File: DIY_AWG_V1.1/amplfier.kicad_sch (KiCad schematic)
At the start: 20 parts, among them IC3 LMH6505MAX, IC4 THS3091DDAR, J4 Conn_Coaxial

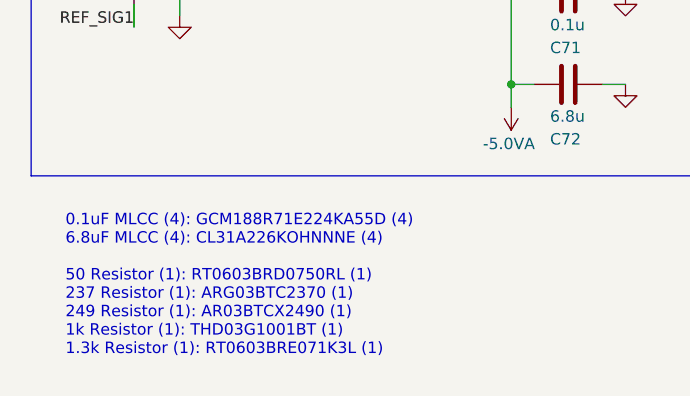
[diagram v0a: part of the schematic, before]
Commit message: Updated amplifier, STM32_MCU schematic
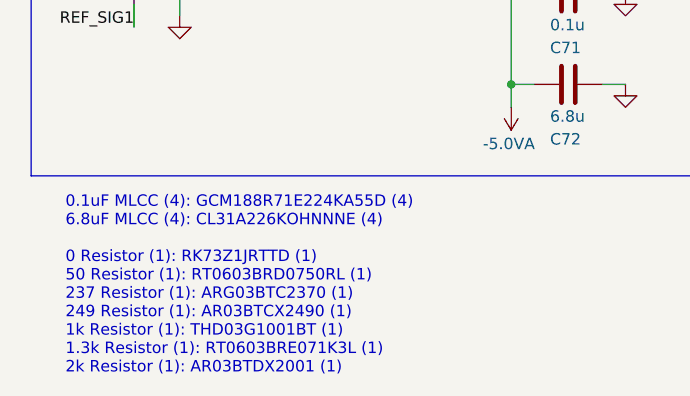
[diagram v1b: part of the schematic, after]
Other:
- note added: "0.1uF MLCC (4): GCM188R71E224KA55D (4) 6.8uF MLCC (4): CL31A226KOHNNNE (4) 0 Resistor (1): RK73Z1JRTTD (1) 50 Resistor (1): RT0603BRD0750RL (1) 237 Resistor (1): ARG03BTC2370 (1) 249 Resistor (1): AR03BTCX2490 (1) 1k Resistor (1): THD03G1001BT (1) 1.3k Resistor (1): RT0603BRE071K3L (1) 2k Resistor (1): AR03BTDX2001 (1)"
- note removed: "0.1uF MLCC (4): GCM188R71E224KA55D (4) 6.8uF MLCC (4): CL31A226KOHNNNE (4) 50 Resistor (1): RT0603BRD0750RL (1) 237 Resistor (1): ARG03BTC2370 (1) 249 Resistor (1): AR03BTCX2490 (1) 1k Resistor (1): THD03G1001BT (1) 1.3k Resistor (1): RT0603BRE071K3L (1)"
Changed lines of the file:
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@@
 		)
 	)
-	(text "0.1uF MLCC (4): GCM188R71E224KA55D (4)\n6.8uF MLCC (4): CL31A226KOHNNNE (4)\n\n50 Resistor (1): RT0603BRD0750RL (1)\n237 Resistor (1): ARG03BTC2370 (1)\n249 Resistor (1): AR03BTCX2490 (1)\n1k Resistor (1): THD03G1001BT (1)\n1.3k Resistor (1): RT0603BRE071K3L (1)"
+	(text "0.1uF MLCC (4): GCM188R71E224KA55D (4)\n6.8uF MLCC (4): CL31A226KOHNNNE (4)\n\n0 Resistor (1): RK73Z1JRTTD (1)\n50 Resistor (1): RT0603BRD0750RL (1)\n237 Resistor (1): ARG03BTC2370 (1)\n249 Resistor (1): AR03BTCX2490 (1)\n1k Resistor (1): THD03G1001BT (1)\n1.3k Resistor (1): RT0603BRE071K3L (1)\n2k Resistor (1): AR03BTDX2001 (1)"
 		(exclude_from_sim no)
 		(at 19.05 88.392 0)

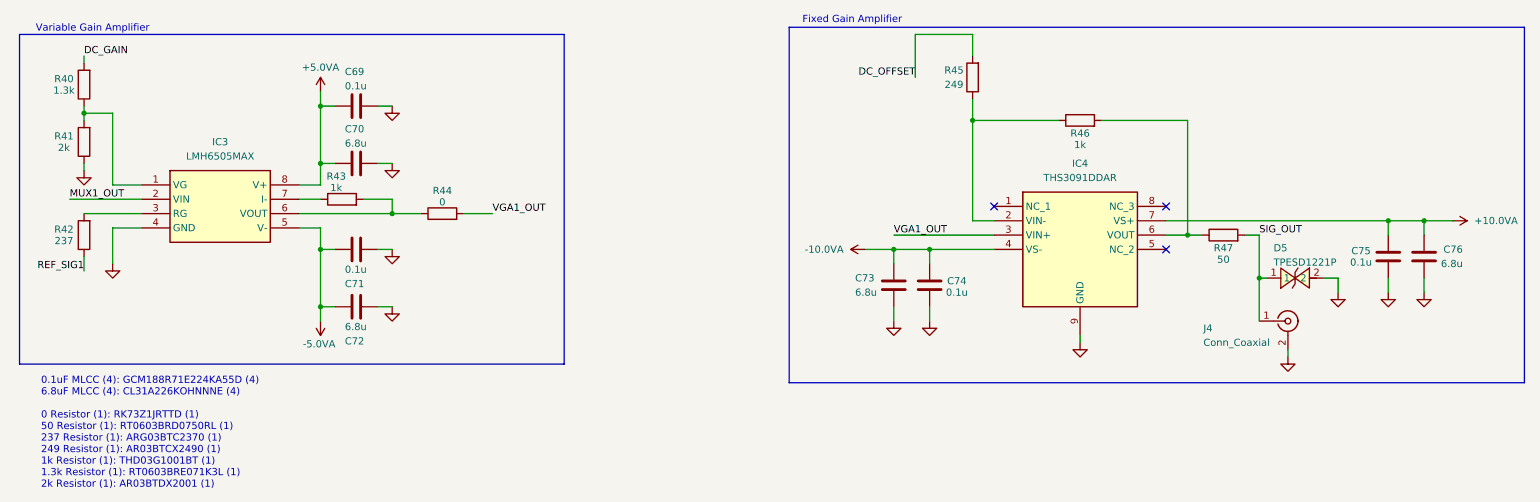
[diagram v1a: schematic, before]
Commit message: Updated STM32_MCU, amplifier schematic
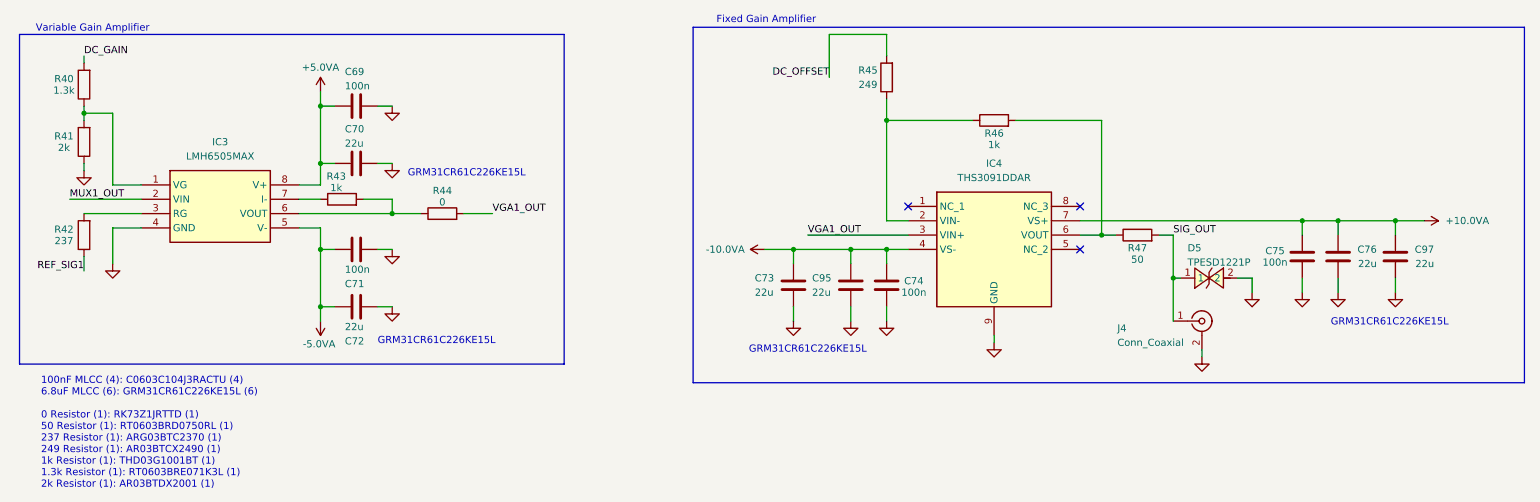
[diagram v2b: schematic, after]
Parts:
- added C95, C97: 22u, symbol Device:C
- C69, C71, C74, C75: value 0.1u -> 100n
- C70, C72, C73, C76: value 6.8u -> 22u
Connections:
- net +10.0VA: now also C97.2
- net -10.0VA: now also C95.2
- net GND: now also C95.1, C97.1
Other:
- note added: "100nF MLCC (4): C0603C104J3RACTU (4) 6.8uF MLCC (6): GRM31CR61C226KE15L (6) 0 Resistor (1): RK73Z1JRTTD (1) 50 Resistor (1): RT0603BRD0750RL (1) 237 Resistor (1): ARG03BTC2370 (1) 249 Resistor (1): AR03BTCX2490 (1) 1k Resistor (1): THD03G1001BT (1) 1.3k Resistor (1): RT0603BRE071K3L (1) 2k Resistor (1): AR03BTDX2001 (1)"
- note added: "GRM31CR61C226KE15L"
- note removed: "0.1uF MLCC (4): GCM188R71E224KA55D (4) 6.8uF MLCC (4): CL31A226KOHNNNE (4) 0 Resistor (1): RK73Z1JRTTD (1) 50 Resistor (1): RT0603BRD0750RL (1) 237 Resistor (1): ARG03BTC2370 (1) 249 Resistor (1): AR03BTCX2490 (1) 1k Resistor (1): THD03G1001BT (1) 1.3k Resistor (1): RT0603BRE071K3L (1) 2k Resistor (1): AR03BTDX2001 (1)"
- moved on the sheet: C73, C74, C75, C76, D5, IC4, J4, R45, R46, R47

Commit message: Updated STM32_MCU, amplifier, User_Interface, AD9834_DDS schematic
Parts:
- renumbered C69 to C82, C70 to C83, C71 to C84, C72 to C85, C73 to C86, C95 to C87, C74 to C88, C75 to C89, C76 to C90, C97 to C91, J4 to J3, R40 to R33, R41 to R34, R42 to R35, R43 to R36, R44 to R37, R45 to R38, R46 to R39, R47 to R40
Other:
- moved on the sheet: C82, C83, C84, C85, IC3, R33, R34, R35, R36, R37

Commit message: Updated all schematics
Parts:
- removed J3: Conn_Coaxial, symbol Connector:Conn_Coaxial
- added RF1: KH-BNC50-3511, easyeda2kicad:ANT-TH_KH-BNC50-3511, symbol easyeda2kicad:KH-BNC50-3511
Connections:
- net GND: now also RF1.2, RF1.3, RF1.4
- net SIG_OUT: now also RF1.1 (OUT)
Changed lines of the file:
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@@
+		(color 0 0 0 0)
+	)
+	(junction
+		(at 224.79 73.66)
+		(diameter 0)
 		(color 0 0 0 0)
 	)
@@
 	(wire
 		(pts
+			(xy 224.79 73.66) (xy 227.33 73.66)
+		)
+		(stroke
+			(width 0)
+			(type default)
+		)
+	)
+	(wire
+		(pts
 			(xy 168.91 17.78) (xy 158.75 17.78)
 		)
@@
 		(pts
 			(xy 162.56 55.88) (xy 168.91 55.88)
+		)
+		(stroke
+			(width 0)
+			(type default)
+		)
+	)
+	(wire
+		(pts
+			(xy 222.25 73.66) (xy 224.79 73.66)
 		)
 		(stroke
@@
 	)
 	(symbol
-		(lib_id "Connector:Conn_Coaxial")
-		(at 224.79 68.58 0)
-		(unit 1)
-		(body_style 1)
-		(exclude_from_sim no)
-		(in_bom yes)
-		(on_board yes)
-		(in_pos_files yes)
-		(dnp no)
-		(property "Reference" "J3"
-			(at 209.804 69.85 0)
-			(show_name no)
-			(do_not_autoplace no)
-			(effects
-				(font
-					(size 1.27 1.27)
-				)
-				(justify left)
-			)
-		)
-		(property "Value" "Conn_Coaxial"
-			(at 209.804 72.39 0)
-			(show_name no)
-			(do_not_autoplace no)
-			(effects
-				(font
-					(size 1.27 1.27)
-				)
-				(justify left)
-			)
-		)
-		(property "Footprint" ""
-			(at 224.79 68.58 0)
-			(hide yes)
-			(show_name no)
-			(do_not_autoplace no)
-			(effects
-				(font
-					(size 1.27 1.27)
-				)
-			)
-		)
-		(property "Datasheet" ""
-			(at 224.79 68.58 0)
-			(hide yes)
-			(show_name no)
-			(do_not_autoplace no)
-			(effects
-				(font
-					(size 1.27 1.27)
-				)
-			)
-		)
-		(property "Description" "coaxial connector (BNC, SMA, SMB, SMC, Cinch/RCA, LEMO, ...)"
-			(at 224.79 68.58 0)
-			(hide yes)
-			(show_name no)
-			(do_not_autoplace no)
-			(effects
-				(font
-					(size 1.27 1.27)
-				)
-			)
-		)
-		(pin "2"
-		)
-		(pin "1"
-		)
-		(instances
-			(project "DIY_AWG_V1.1"
-				(path "/508078af-d961-4af3-840e-a064a9f8d5bc/faa0e7f2-4ad4-4392-8346-980541b6a840"
-					(reference "J3")
-					(unit 1)
-				)
-			)
-		)
-	)
-	(symbol
 		(lib_id "Device:C")
 		(at 162.56 62.23 0)
@@
 					(unit 1)
 				)
+			)
+		)
+	)
+	(symbol
+		(lib_id "easyeda2kicad:KH-BNC50-3511")
+		(at 223.52 69.85 0)
+		(mirror y)
+		(unit 1)
+		(body_style 1)
+		(exclude_from_sim no)
+		(in_bom yes)
+		(on_board yes)
+		(in_pos_files yes)
+		(dnp no)
+		(property "Reference" "RF1"
+			(at 228.6 69.8501 0)
+			(show_name no)
+			(do_not_autoplace no)
+			(effects
+				(font
+					(size 1.27 1.27)
+				)
+				(justify right)
+			)
+		)
+		(property "Value" "KH-BNC50-3511"
+			(at 228.6 67.3101 0)
+			(show_name no)
+			(do_not_autoplace no)
+			(effects
+				(font
+					(size 1.27 1.27)
+				)
+				(justify right)
+			)
+		)
+		(property "Footprint" "easyeda2kicad:ANT-TH_KH-BNC50-3511"
+			(at 223.52 81.28 0)
+			(hide yes)
+			(show_name no)
+			(do_not_autoplace no)
+			(effects
+				(font
+					(size 1.27 1.27)
+				)
+			)
+		)
+		(property "Datasheet" "https://www.lcsc.com/datasheet/C2837587.pdf"
+			(at 223.52 83.82 0)
+			(hide yes)
+			(show_name no)
+			(do_not_autoplace no)
+			(effects
+				(font
+					(size 1.27 1.27)
+				)
+			)
+		)
+		(property "Description" ""
+			(at 223.52 69.85 0)
+			(hide yes)
+			(show_name no)
+			(do_not_autoplace no)
+			(effects
+				(font
+					(size 1.27 1.27)
+				)
+			)
+		)
+		(property "Manufacturer" "kinghelm(金航标)"
+			(at 223.52 86.36 0)
+			(hide yes)
+			(show_name no)
+			(do_not_autoplace no)
+			(effects
+				(font
+					(size 1.27 1.27)
+				)
+			)
+		)
+		(property "MPN" "KH-BNC50-3511"
+			(at 223.52 88.9 0)
+			(hide yes)
+			(show_name no)
+			(do_not_autoplace no)
+			(effects
+				(font
+					(size 1.27 1.27)
+				)
+			)
+		)
+		(property "LCSC Part" "C2837587"
+			(at 223.52 91.44 0)
+			(hide yes)
+			(show_name no)
+			(do_not_autoplace no)
+			(effects
+				(font
+					(size 1.27 1.27)
+				)
+			)
+		)
+		(pin "1"
+		)
+		(pin "3"
+		)
+		(pin "2"
+		)
+		(pin "4"
+		)
+		(instances
+			(project "DIY_AWG_V1.1"
+				(path "/508078af-d961-4af3-840e-a064a9f8d5bc/faa0e7f2-4ad4-4392-8346-980541b6a840"
+					(reference "RF1")
+					(unit 1)
+				)

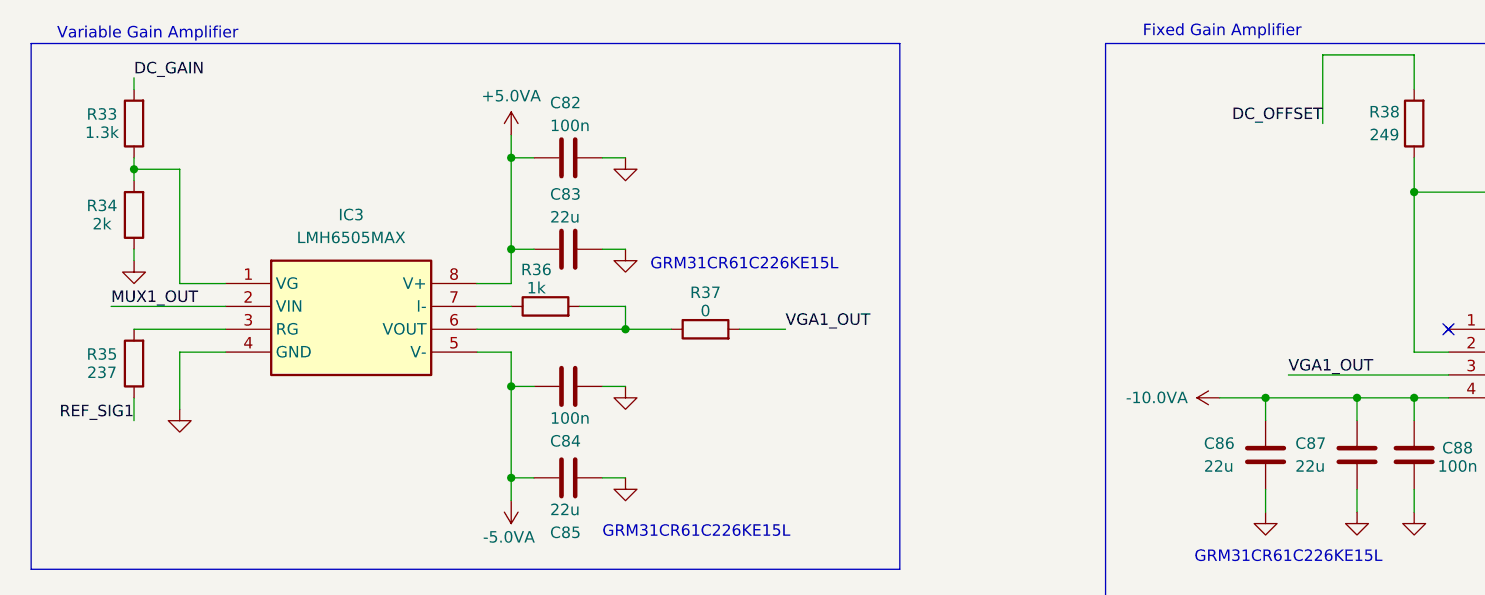
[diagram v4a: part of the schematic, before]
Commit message: Updated pin description of relevant components
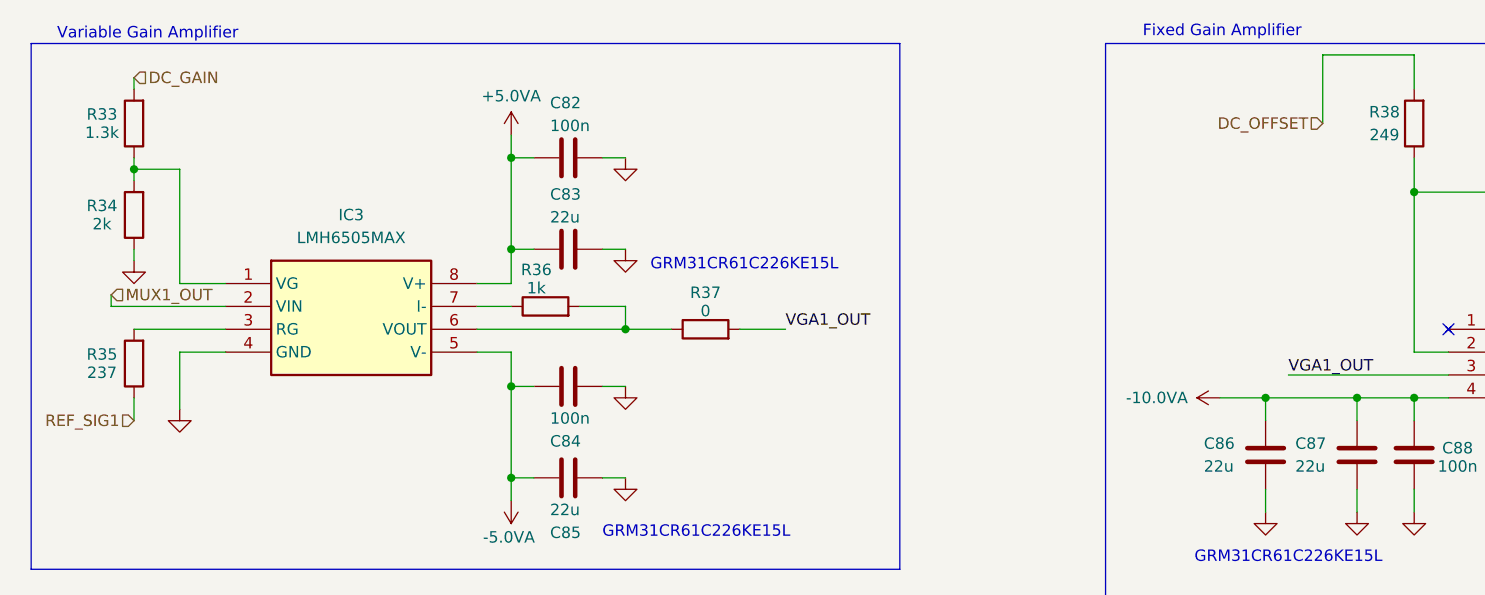
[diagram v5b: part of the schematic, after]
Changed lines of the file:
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@@
+	(wire
+		(pts
+			(xy 24.13 44.45) (xy 24.13 45.72)
+		)
+		(stroke
+			(width 0)
+			(type default)
+		)
+	)
 	(wire
 		(pts
@@
 		)
 	)
-	(label "DC_OFFSET"
-		(at 158.75 25.4 180)
-		(effects
-			(font
-				(size 1.27 1.27)
-			)
-			(justify right bottom)
-		)
-	)
-	(label "DC_GAIN"
-		(at 26.67 20.32 0)
-		(effects
-			(font
-				(size 1.27 1.27)
-			)
-			(justify left bottom)
-		)
-	)
-	(label "MUX1_OUT"
-		(at 24.13 45.72 0)
-		(effects
-			(font
-				(size 1.27 1.27)
-			)
-			(justify left bottom)
-		)
-	)
-	(label "REF_SIG1"
-		(at 26.67 58.42 180)
-		(effects
-			(font
-				(size 1.27 1.27)
-			)
-			(justify right bottom)
-		)
-	)
 	(label "SIG_OUT"
 		(at 219.71 53.34 0)
@@
 		)
 	)
+	(hierarchical_label "REF_SIG1"
+		(shape input)
+		(at 26.67 58.42 180)
+		(effects
+			(font
+				(size 1.27 1.27)
+			)
+			(justify right)
+		)
+	)
+	(hierarchical_label "MUX1_OUT"
+		(shape input)
+		(at 24.13 44.45 0)
+		(effects
+			(font
+				(size 1.27 1.27)
+			)
+			(justify left)
+		)
+	)
+	(hierarchical_label "DC_GAIN"
+		(shape input)
+		(at 26.67 20.32 0)
+		(effects
+			(font
+				(size 1.27 1.27)
+			)
+			(justify left)
+		)
+	)
+	(hierarchical_label "DC_OFFSET"
+		(shape input)
+		(at 158.75 25.4 180)
+		(effects
+			(font
+				(size 1.27 1.27)
+			)
+			(justify right)
+		)
+	)

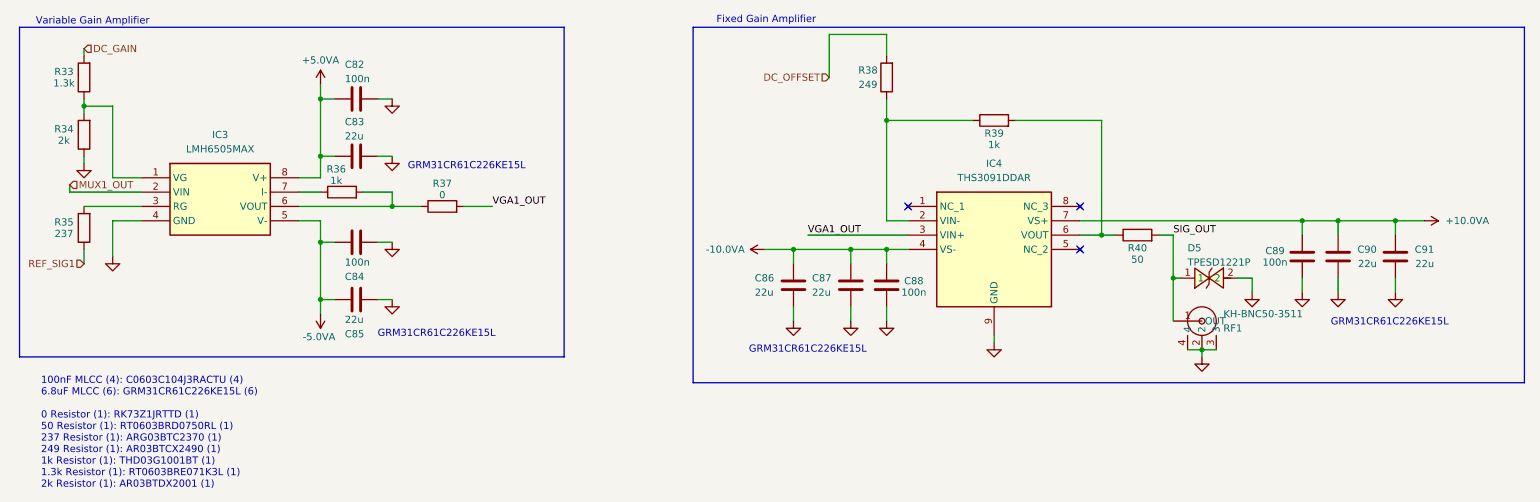
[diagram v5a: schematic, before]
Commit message: Updated schematics to clear ERCs
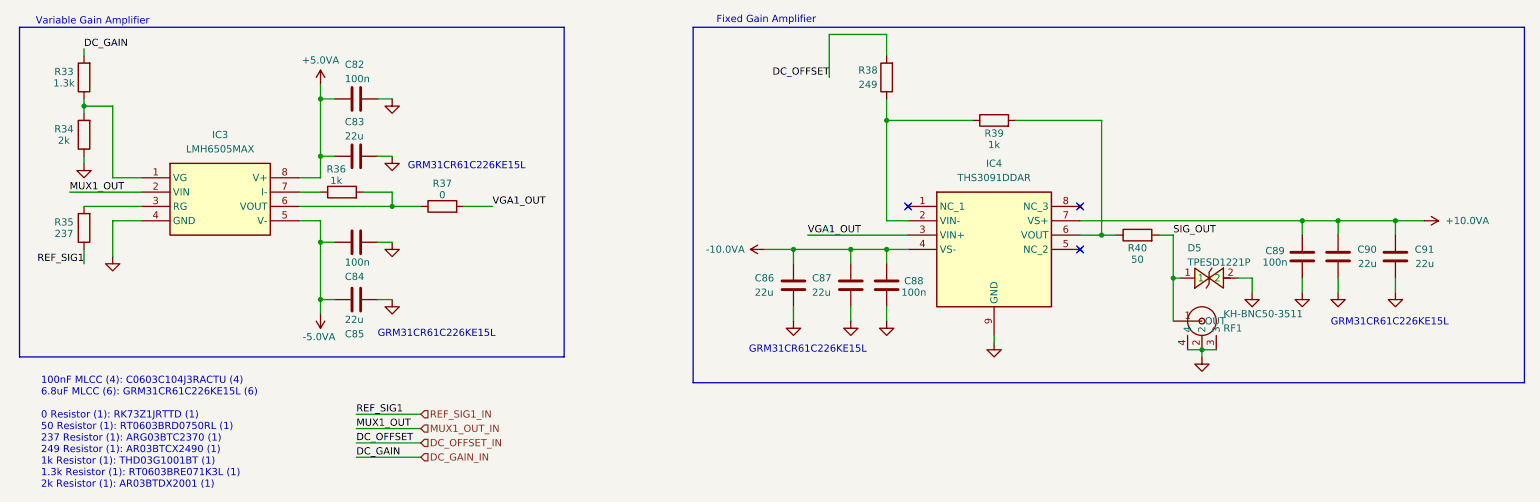
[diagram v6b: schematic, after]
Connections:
- net DC_GAIN renamed DC_GAIN_IN
- net DC_OFFSET renamed DC_OFFSET_IN
- net MUX1_OUT renamed MUX1_OUT_IN
- net REF_SIG1 renamed REF_SIG1_IN
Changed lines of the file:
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@@
+	(wire
+		(pts
+			(xy 74.93 85.09) (xy 86.36 85.09)
+		)
+		(stroke
+			(width 0)
+			(type default)
+		)
+	)
 	(wire
 		(pts
@@
 	(wire
 		(pts
+			(xy 74.93 90.17) (xy 86.36 90.17)
+		)
+		(stroke
+			(width 0)
+			(type default)
+		)
+	)
+	(wire
+		(pts
+			(xy 74.93 92.71) (xy 86.36 92.71)
+		)
+		(stroke
+			(width 0)
+			(type default)
+		)
+	)
+	(wire
+		(pts
 			(xy 233.68 63.5) (xy 233.68 60.96)
 		)
@@
 	(wire
 		(pts
+			(xy 74.93 87.63) (xy 86.36 87.63)
+		)
+		(stroke
+			(width 0)
+			(type default)
+		)
+	)
+	(wire
+		(pts
 			(xy 152.4 55.88) (xy 152.4 58.42)
 		)
@@
 		(pts
 			(xy 26.67 48.26) (xy 36.83 48.26)
-		)
-		(stroke
-			(width 0)
-			(type default)
-		)
-	)
-	(wire
-		(pts
-			(xy 24.13 44.45) (xy 24.13 45.72)
 		)
 		(stroke
@@
 		)
 	)
+	(label "MUX1_OUT"
+		(at 24.13 45.72 0)
+		(effects
+			(font
+				(size 1.27 1.27)
+			)
+			(justify left bottom)
+		)
+	)
+	(label "DC_GAIN"
+		(at 26.67 20.32 0)
+		(effects
+			(font
+				(size 1.27 1.27)
+			)
+			(justify left bottom)
+		)
+	)
 	(label "VGA1_OUT"
 		(at 154.94 53.34 0)
@@
 		)
 	)
+	(label "MUX1_OUT"
+		(at 74.93 87.63 0)
+		(effects
+			(font
+				(size 1.27 1.27)
+			)
+			(justify left bottom)
+		)
+	)
+	(label "DC_OFFSET"
+		(at 158.75 25.4 180)
+		(effects
+			(font
+				(size 1.27 1.27)
+			)
+			(justify right bottom)
+		)
+	)
+	(label "DC_OFFSET"
+		(at 74.93 90.17 0)
+		(effects
+			(font
+				(size 1.27 1.27)
+			)
+			(justify left bottom)
+		)
+	)
+	(label "REF_SIG1"
+		(at 26.67 58.42 180)
+		(effects
+			(font
+				(size 1.27 1.27)
+			)
+			(justify right bottom)
+		)
+	)
 	(label "SIG_OUT"
 		(at 219.71 53.34 0)
@@
 		)
 	)
-	(hierarchical_label "REF_SIG1"
+	(label "DC_GAIN"
+		(at 74.93 92.71 0)
+		(effects
+			(font
+				(size 1.27 1.27)
+			)
+			(justify left bottom)
+		)
+	)
+	(label "REF_SIG1"
+		(at 74.93 85.09 0)
+		(effects
+			(font
+				(size 1.27 1.27)
+			)
+			(justify left bottom)
+		)
+	)
+	(hierarchical_label "REF_SIG1_IN"
 		(shape input)
-		(at 26.67 58.42 180)
-		(effects
-			(font
-				(size 1.27 1.27)
-			)
-			(justify right)
-		)
-	)
-	(hierarchical_label "MUX1_OUT"
+		(at 86.36 85.09 0)
+		(effects
+			(font
+				(size 1.27 1.27)
+			)
+			(justify left)
+		)
+	)
+	(hierarchical_label "MUX1_OUT_IN"
 		(shape input)
-		(at 24.13 44.45 0)
+		(at 86.36 87.63 0)
 		(effects
 			(font
@@
 		)
 	)
-	(hierarchical_label "DC_GAIN"
+	(hierarchical_label "DC_OFFSET_IN"
 		(shape input)
-		(at 26.67 20.32 0)
+		(at 86.36 90.17 0)
 		(effects
 			(font
@@
 		)
 	)
-	(hierarchical_label "DC_OFFSET"
+	(hierarchical_label "DC_GAIN_IN"
 		(shape input)
-		(at 158.75 25.4 180)
-		(effects
-			(font
-				(size 1.27 1.27)
-			)
-			(justify right)
-		)
-	)
+		(at 86.36 92.71 0)
+		(effects
+			(font
+				(size 1.27 1.27)
+			)
+			(justify left)
+		)
+	)
